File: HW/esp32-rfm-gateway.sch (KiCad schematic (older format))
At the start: 57 parts, among them J1 Res, J2 Boot, J20 220V~, J21 c5V, J22 s14500, J23 s18650, J24 cPS, J3 PinDbg, J30 AntSMA, J4 PinsI2C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

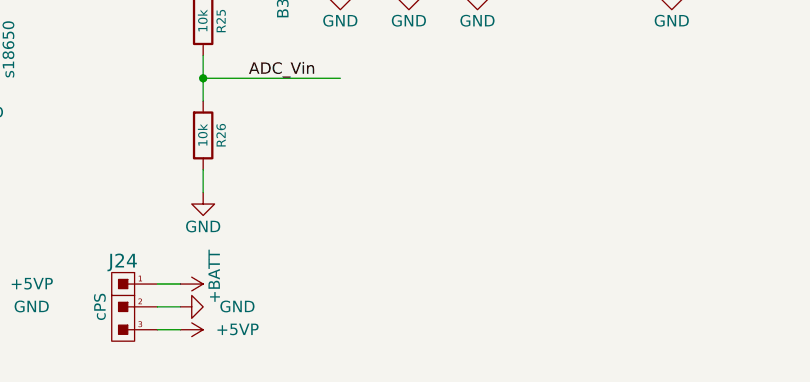
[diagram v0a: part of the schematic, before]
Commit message: Adds a 3.3V header as placeholder in the power section
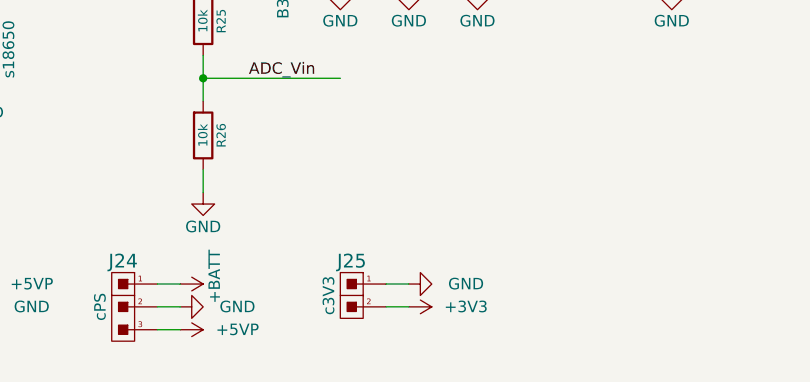
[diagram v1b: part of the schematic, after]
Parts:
- added J25: c3V3, CalinConnectors:Pin_Header_Angled_1x02, symbol calin:CS_2s
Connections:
- wire segments 210 -> 212
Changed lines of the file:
@@
 Title "ESP32 RFM69/RFM9x Gateway"
 Date "2019-04-13"
-Rev "11"
+Rev "12"
 Comp "Calin Radoni"
 Comment1 ""
@@
 Wire Wire Line
 	4200 7000 4300 7000
+$Comp
+L calin:CS_2s J25
+U 1 1 5CB55B01
+P 5050 6850
+F 0 "J25" H 5050 7000 60  0000 C CNN
+F 1 "c3V3" V 5150 6850 50  0000 C CNN
+F 2 "CalinConnectors:Pin_Header_Angled_1x02" H 5050 6900 60  0001 C CNN
+F 3 "" H 5050 6900 60  0000 C CNN
+	1    5050 6850
+	-1   0    0    -1
+$EndComp
+$Comp
+L power:GND #PWR0147
+U 1 1 5CB55BCE
+P 5300 6800
+F 0 "#PWR0147" H 5300 6550 50  0001 C CNN
+F 1 "GND" V 5300 6550 50  0000 C CNN
+F 2 "" H 5300 6800 50  0000 C CNN
+F 3 "" H 5300 6800 50  0000 C CNN
+	1    5300 6800
+	0    -1   -1   0
+$EndComp
+$Comp
+L power:+3V3 #PWR0148
+U 1 1 5CB55E09
+P 5300 6900
+F 0 "#PWR0148" H 5300 6750 50  0001 C CNN
+F 1 "+3V3" V 5300 7150 50  0000 C CNN
+F 2 "" H 5300 6900 50  0000 C CNN
+F 3 "" H 5300 6900 50  0000 C CNN
+	1    5300 6900
+	0    1    1    0
+$EndComp
+Wire Wire Line
+	5300 6800 5200 6800
+Wire Wire Line
+	5200 6900 5300 6900
 $EndSCHEMATC

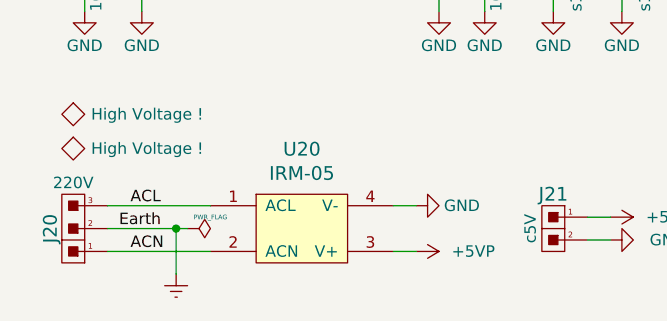
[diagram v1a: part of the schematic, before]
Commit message: Adds an Earth screw hole and changes the High Voltage symbol
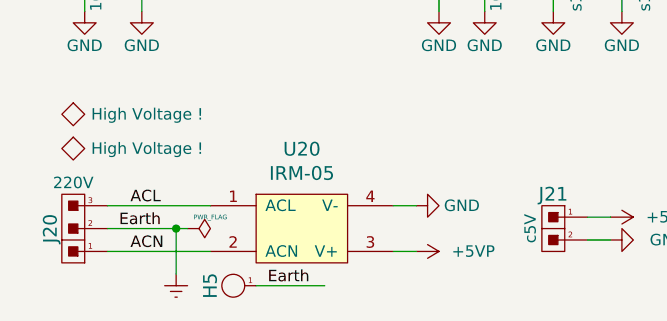
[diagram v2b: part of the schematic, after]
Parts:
- added H5: HolePlated, CalinGeneric:HolePlated-M2.5, symbol calin:HolePlated
- SYM3, SYM4: footprint Symbol:Symbol_HighVoltage_Type1_CopperTop_Big -> CalinGeneric:Symbol_HighVoltage_SilkS
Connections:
- wire segments 212 -> 213
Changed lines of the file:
@@
 Title "ESP32 RFM69/RFM9x Gateway"
 Date "2019-04-13"
-Rev "12"
+Rev "14"
 Comp "Calin Radoni"
 Comment1 ""
@@
 F 0 "SYM3" H 1200 6350 50  0001 C CNN
 F 1 "High Voltage !" H 1128 6350 50  0000 L CNN
-F 2 "Symbol:Symbol_HighVoltage_Type1_CopperTop_Big" H 1050 6350 50  0001 C CNN
+F 2 "CalinGeneric:Symbol_HighVoltage_SilkS" H 1050 6350 50  0001 C CNN
 F 3 "" V 1050 6350 50  0001 C CNN
 	1    1050 6350
@@
 F 0 "SYM4" H 1200 6500 50  0001 C CNN
 F 1 "High Voltage !" H 1128 6500 50  0000 L CNN
-F 2 "Symbol:Symbol_HighVoltage_Type1_CopperTop_Big" H 1050 6500 50  0001 C CNN
+F 2 "CalinGeneric:Symbol_HighVoltage_SilkS" H 1050 6500 50  0001 C CNN
 F 3 "" V 1050 6500 50  0001 C CNN
 	1    1050 6500
@@
 Wire Wire Line
 	5200 6900 5300 6900
+$Comp
+L calin:HolePlated H5
+U 1 1 5CB7E46D
+P 1750 7100
+F 0 "H5" H 1750 7200 60  0000 C CNN
+F 1 "HolePlated" H 1750 7000 60  0001 C CNN
+F 2 "CalinGeneric:HolePlated-M2.5" H 1750 7100 60  0001 C CNN
+F 3 "" H 1750 7100 60  0000 C CNN
+	1    1750 7100
+	0    -1   -1   0
+$EndComp
+Wire Wire Line
+	1850 7100 2150 7100
+Text Label 1900 7100 0    50   ~ 0
+Earth
 $EndSCHEMATC

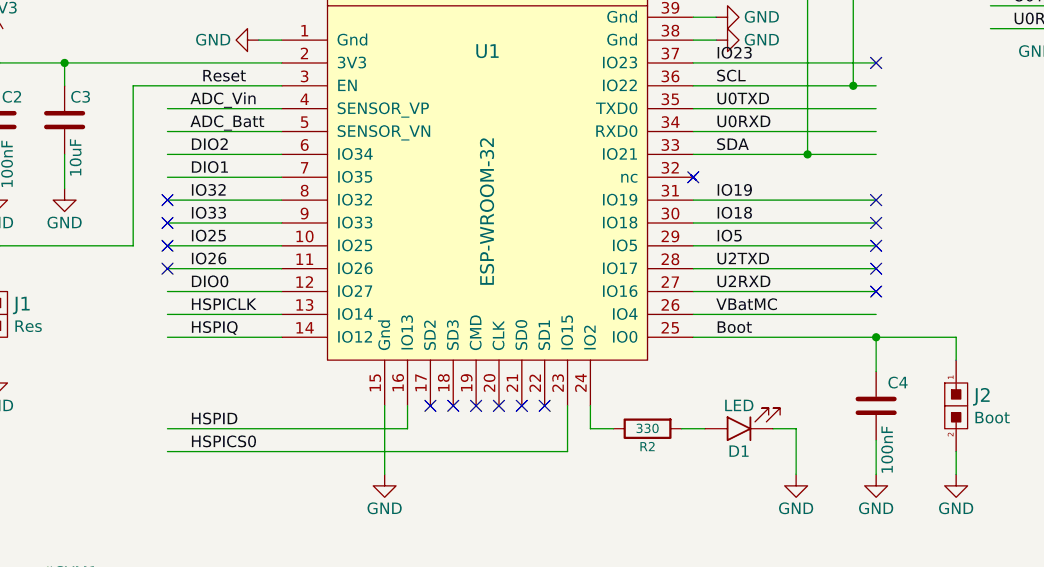
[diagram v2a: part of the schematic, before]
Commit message: Connects VBatMC to IO26 and move battery to the right
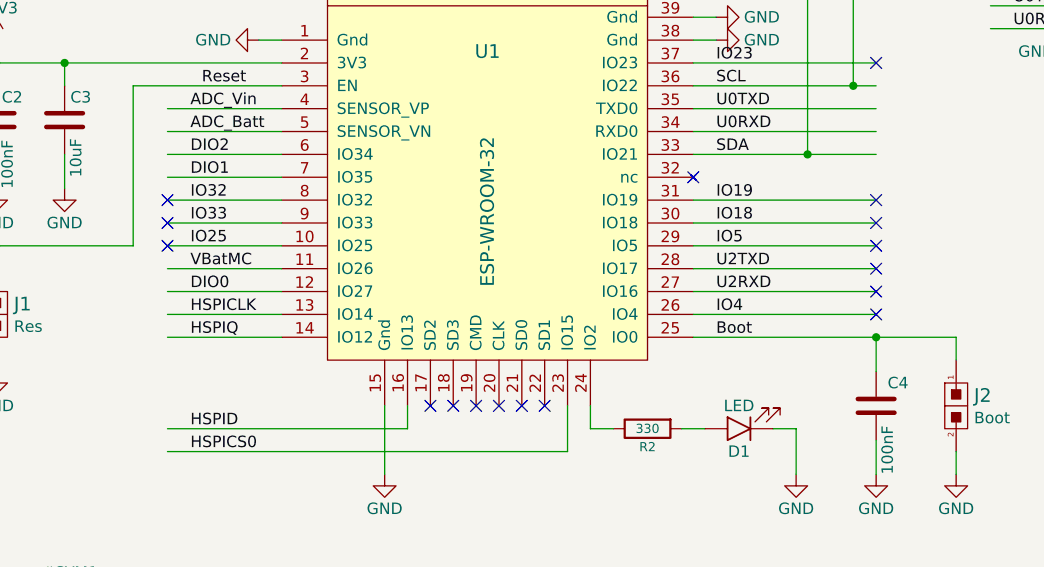
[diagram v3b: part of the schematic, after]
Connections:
- net labels added: IO4
- net labels removed: IO26
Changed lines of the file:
@@
 Title "ESP32 RFM69/RFM9x Gateway"
 Date "2019-04-13"
-Rev "14"
+Rev "15"
 Comp "Calin Radoni"
 Comment1 ""
@@
 Text Label 3150 2700 0    50   ~ 0
 DIO0
-Text Label 3150 2600 0    50   ~ 0
-IO26
 Text Label 3150 2500 0    50   ~ 0
 IO25
@@
 Text Label 6750 1550 0    50   ~ 0
 U0RXD
-Text Label 5450 2800 0    50   ~ 0
+Text Label 3150 2600 0    50   ~ 0
 VBatMC
 Wire Wire Line
@@
 NoConn ~ 3050 2400
 NoConn ~ 3050 2500
-NoConn ~ 3050 2600
 $Comp
 L calin:CS_5 J30
@@
 Text Label 1900 7100 0    50   ~ 0
 Earth
+NoConn ~ 6150 2800
+Text Label 5450 2800 0    50   ~ 0
+IO4
 $EndSCHEMATC

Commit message: Changes a lot of signals and connections, still a work in progress ...
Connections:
- net labels removed: IO25, IO32, IO33
- wire segments 213 -> 211
- no-connect marks 21 -> 20
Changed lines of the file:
@@
 Title "ESP32 RFM69/RFM9x Gateway"
 Date "2019-04-13"
-Rev "15"
+Rev "16"
 Comp "Calin Radoni"
 Comment1 ""
@@
 	3550 2400 3050 2400
 Text Label 3150 2700 0    50   ~ 0
-DIO0
-Text Label 3150 2500 0    50   ~ 0
-IO25
-Text Label 3150 2400 0    50   ~ 0
-IO33
+DIO2
 $Comp
 L calin:R R2
@@
 Wire Wire Line
 	3550 2300 3050 2300
-Text Label 3150 2300 0    50   ~ 0
-IO32
 $Comp
 L calin:LED D1
@@
 Wire Wire Line
 	3550 2000 3050 2000
-Wire Wire Line
-	3550 2100 3050 2100
-Wire Wire Line
-	3550 2200 3050 2200
+Text Label 3150 2000 0    50   ~ 0
+ADC_Vin
 Text Label 3150 1900 0    50   ~ 0
-ADC_Vin
-Text Label 3150 2000 0    50   ~ 0
 ADC_Batt
-Text Label 3150 2100 0    50   ~ 0
-DIO2
-Text Label 3150 2200 0    50   ~ 0
+Text Label 3150 2500 0    50   ~ 0
+DIO0
+Text Label 3150 2600 0    50   ~ 0
 DIO1
 Wire Wire Line
@@
 Text Label 6750 1550 0    50   ~ 0
 U0RXD
-Text Label 3150 2600 0    50   ~ 0
+Text Label 3150 2400 0    50   ~ 0
 VBatMC
 Wire Wire Line
@@
 NoConn ~ 6150 2600
 NoConn ~ 6150 2700
-NoConn ~ 3050 2300
-NoConn ~ 3050 2400
-NoConn ~ 3050 2500
 $Comp
 L calin:CS_5 J30
@@
 Text Label 2850 4900 0    50   ~ 0
 ChargeStat
-Text Label 4750 4000 0    50   ~ 0
+Text Label 3150 2300 0    50   ~ 0
 ChargeStat
 $Comp
@@
 Text Label 5450 2800 0    50   ~ 0
 IO4
+NoConn ~ 3550 2100
+NoConn ~ 3550 2200
 $EndSCHEMATC
